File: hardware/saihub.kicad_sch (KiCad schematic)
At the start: 55 parts, among them J1 USB4105-GF-A, J2 1x12 2.54mm right-angle, Q1 AO3400A, SW1 BOOT, U1 USBLC6-2SC6, U2 SGM6232YPS8G/TR, U3 ESPC5-32E-H4, U4 TPS2553DBVR, U5 TPS2553DBVR

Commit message: feat(hardware): add header protection and refresh board deliverables
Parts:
- removed R13, R14: 10k, Saihub:R_0603_1608Metric, symbol Saihub:R
- added C21: 100n, Saihub:C_0603_1608Metric, symbol Saihub:C
- added U10: USBLC6-2SC6, Saihub:SOT-23-6, symbol Saihub:USBLC6_2SC6
- added U6, U7: TPD4E05U06DQAR, Saihub:TPD4E05U06_DQA, symbol Saihub:TPD4E05U06
- D3: value SS14 -> SS34; MPN SS14 -> SS34
- R10, R12, R9: value 100k -> 10k; MPN 100k -> 10k
- U4, U5: value TPS2553DBVR -> TPS2553DDBVR; MPN TPS2553DBVR -> TPS2553DDBVR
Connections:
- net FAULT4: now also U3.19 (GPIO15)
- net FAULT5: now also U3.5 (GPIO3)
- net GND: now also C21.2, U10.2 (GND), U6.3 (GND), U6.8 (GND), U7.3 (GND), U7.8 (GND)
- net IO0: now also U6.1 (IO1)
- net IO1: now also U6.2 (IO2)
- net IO2: now also U6.4 (IO3)
- net IO3: now also U6.5 (IO4)
- net IO4: now also U7.1 (IO1)
- net IO5: now also U7.2 (IO2)
- net IO6: now also U7.4 (IO3)
- net IO7: now also U7.5 (IO4)
- net V3_SW: now also U10.1 (IO1), U10.6 (IO1)
- net V5: now also C21.1, U10.5 (VBUS)
- net V5_SW: now also U10.3 (IO2), U10.4 (IO2)
- no-connect marks 12 -> 18
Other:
- note added: "07 HEADER ESD / SHUNT PROTECTION"
- note added: "48 x 28 mm PCB - top-side component assembly."
- note added: "FAULT4 -> input 15; FAULT5 -> input 3. Active LOW."
- note added: "Fault inputs: firmware must enable internal pullups."
- note added: "IO0-IO7: 3.3 V only; final-board ESD test required."
- note added: "Place arrays and bypass capacitors directly beside J2."
- note added: "Short, wide ground returns; qualify ESD on final PCB."
- note added: "U10: switched rails. Power current bypasses the array."
- note added: "U6/U7: four channels each; no supply or bypass needed."

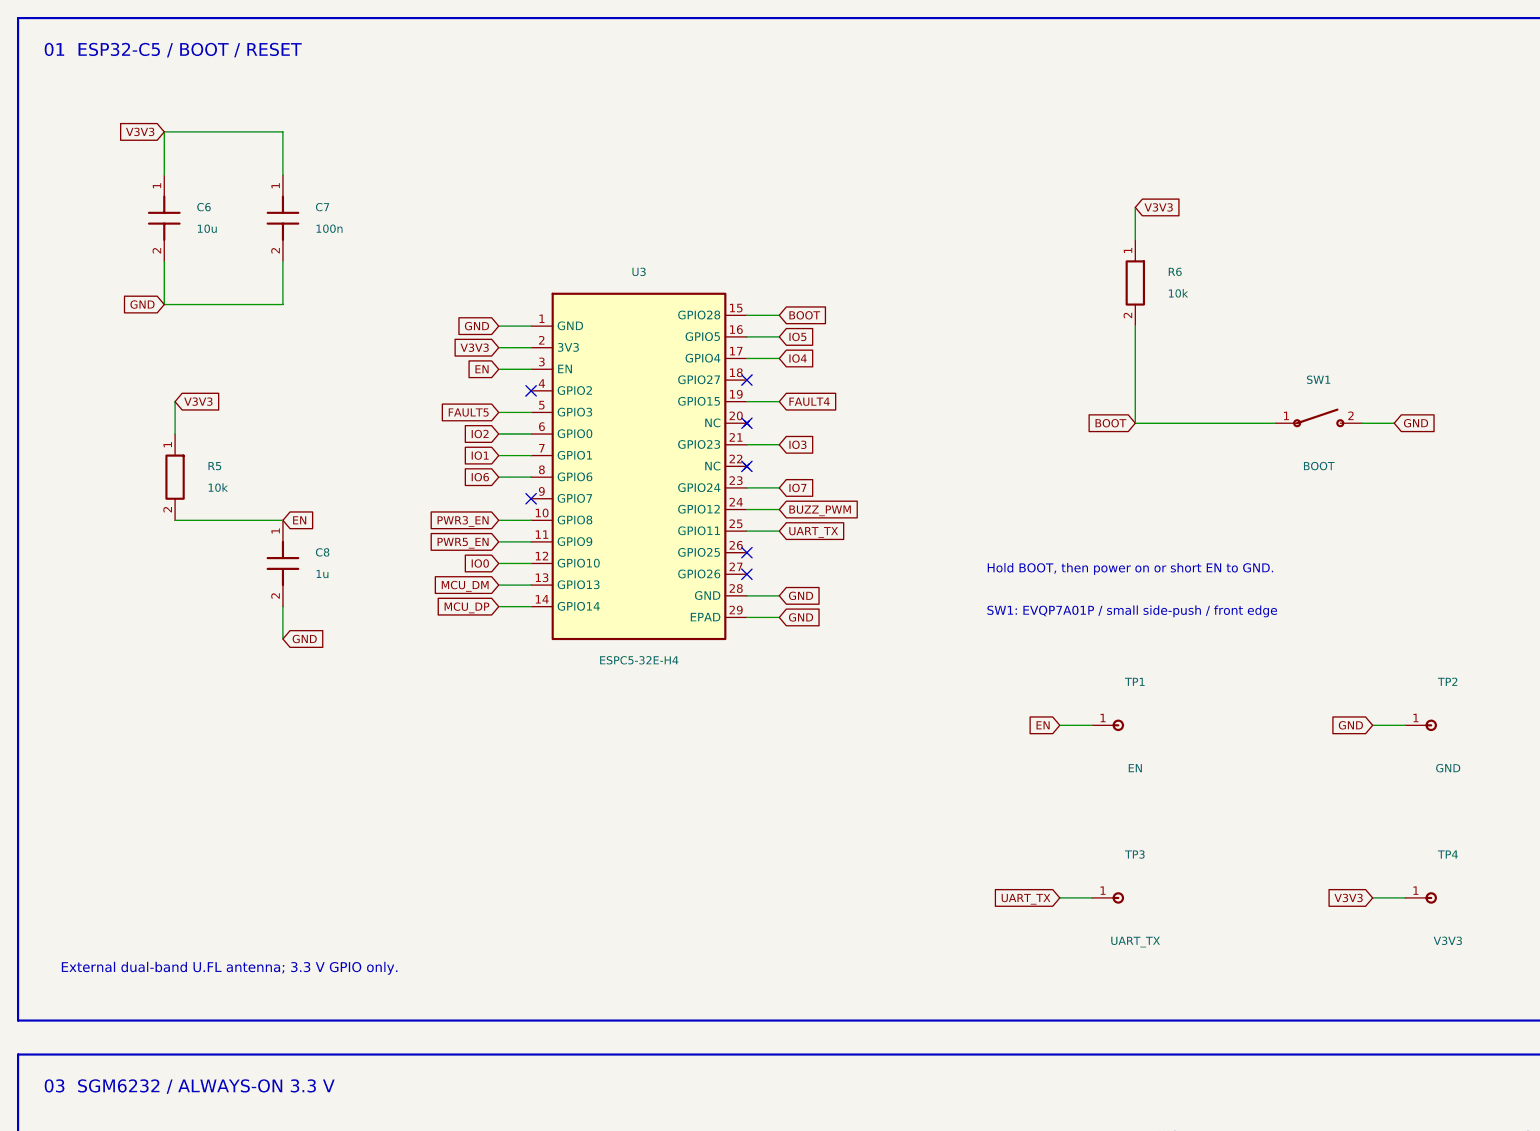
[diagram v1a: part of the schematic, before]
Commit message: Replace button and add corner antenna module without enlarging PCB
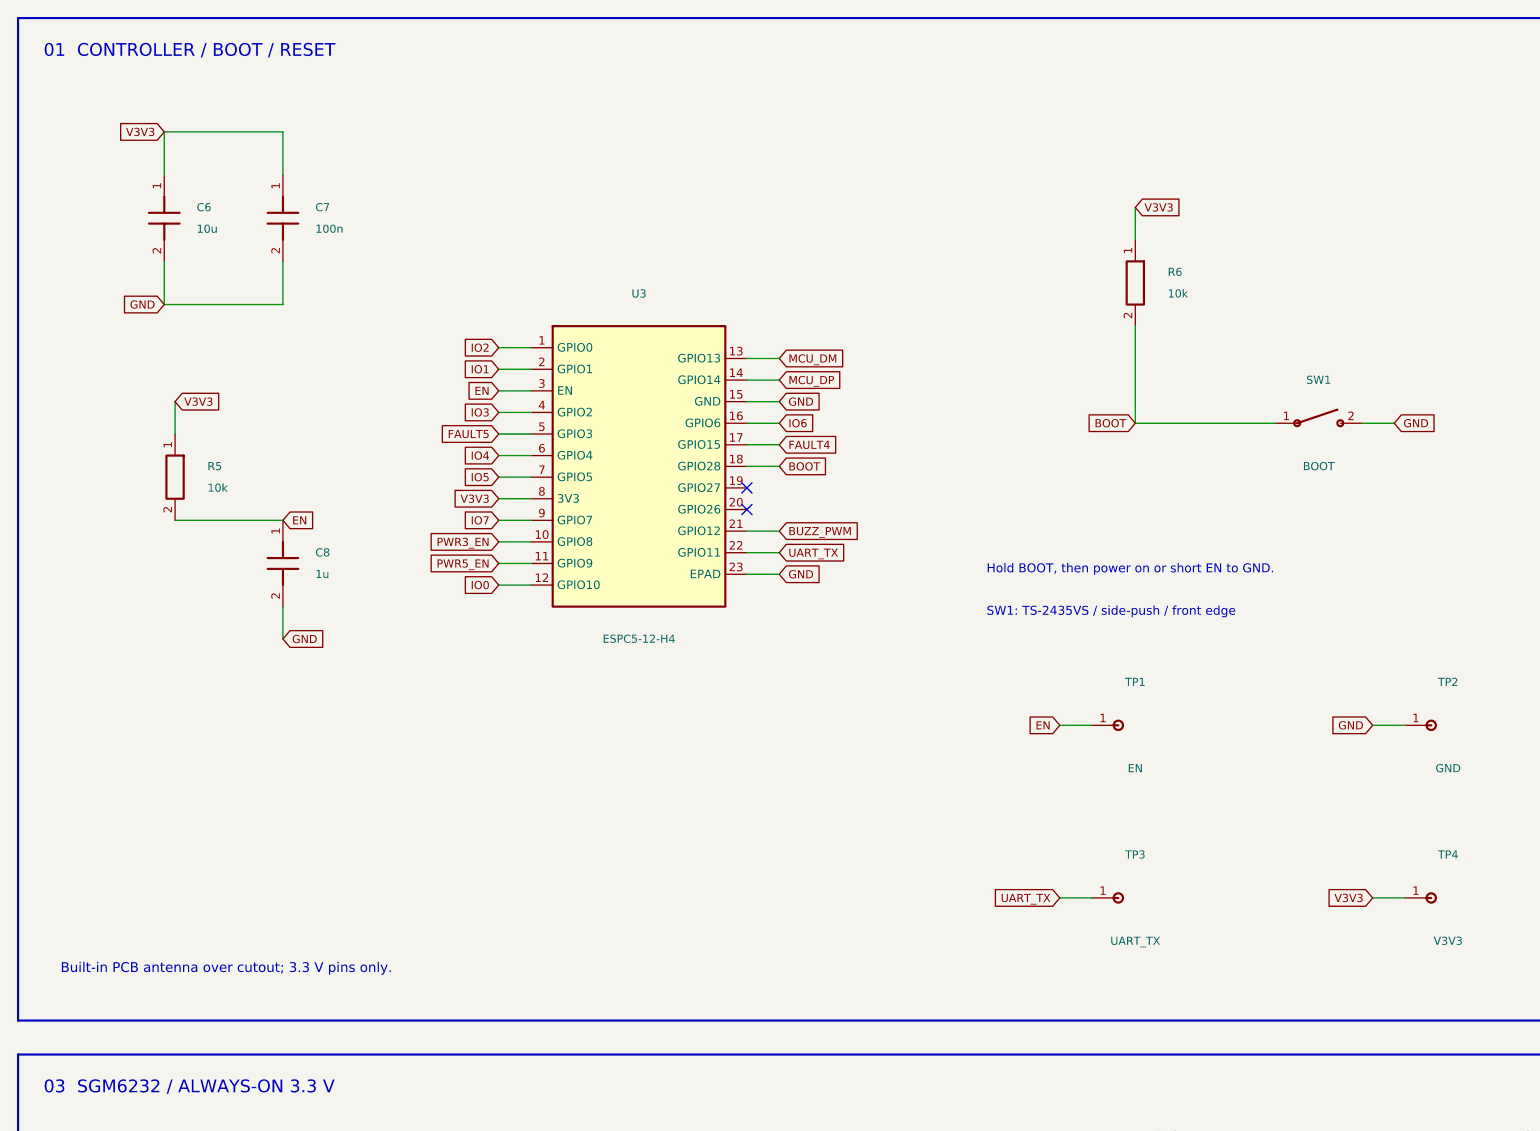
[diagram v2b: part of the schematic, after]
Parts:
- SW1: footprint Saihub:SW_SPST_EVQP7A -> Saihub:SW_SPST_TS2435VS; MPN EVQP7A01P -> TS-2435VS
- U3: value ESPC5-32E-H4 -> ESPC5-12-H4; footprint Saihub:ESPC5-32E-H4 -> Saihub:ESPC5-12-H4; symbol Saihub:ESPC5_32E_H4 -> Saihub:ESPC5_12_H4; MPN ESPC5-32E-H4 -> ESPC5-12-H4
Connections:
- net BOOT: now also U3.18 (GPIO28); no longer U3.15 (GPIO28)
- net BUZZ_PWM: now also U3.21 (GPIO12); no longer U3.24 (GPIO12)
- net FAULT4: now also U3.17 (GPIO15); no longer U3.19 (GPIO15)
- net GND: now also U3.15 (GND), U3.23 (EPAD); no longer U3.1 (GND), U3.28 (GND), U3.29 (EPAD)
- net IO1: now also U3.2 (GPIO1); no longer U3.7 (GPIO1)
- net IO2: now also U3.1 (GPIO0); no longer U3.6 (GPIO0)
- net IO3: now also U3.4 (GPIO2); no longer U3.21 (GPIO23)
- net IO4: now also U3.6 (GPIO4); no longer U3.17 (GPIO4)
- net IO5: now also U3.7 (GPIO5); no longer U3.16 (GPIO5)
- net IO6: now also U3.16 (GPIO6); no longer U3.8 (GPIO6)
- net IO7: now also U3.9 (GPIO7); no longer U3.23 (GPIO24)
- net UART_TX: now also U3.22 (GPIO11); no longer U3.25 (GPIO11)
- net V3V3: now also U3.8 (3V3); no longer U3.2 (3V3)
- no-connect marks 18 -> 13
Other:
- note added: "01 CONTROLLER / BOOT / RESET"
- note added: "Built-in PCB antenna over cutout; 3.3 V pins only."
- note added: "SW1: TS-2435VS / side-push / front edge"
- note removed: "01 ESP32-C5 / BOOT / RESET"
- note removed: "External dual-band U.FL antenna; 3.3 V GPIO only."
- note removed: "SW1: EVQP7A01P / small side-push / front edge"
- title: SAIHub-Mini - ESP32-C5 GPIO CONTROLLER -> SAIHub-Mini - IO CONTROLLER

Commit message: feat(hardware): add grouped indicators and reproducible routing
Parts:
- added D4, D5: GREEN, Saihub:LED_AA1608, symbol Saihub:LED
- added D6: RED, Saihub:LED_AA1608, symbol Saihub:LED
- added D7: BLUE, Saihub:LED_AA1608, symbol Saihub:LED
- added R19: 680, Saihub:R_0603_1608Metric, symbol Saihub:R
- added R20, R21: 1.5k, Saihub:R_0603_1608Metric, symbol Saihub:R
- added R22: 330, Saihub:R_0603_1608Metric, symbol Saihub:R
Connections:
- net GND: now also D4.1 (K), D5.1 (K), D6.1 (K), D7.1 (K)
- net V3_SW: now also R19.1
- net V5: now also R21.1
- net V5_SW: now also R20.1
- net STATUS_LED: now reaches U3.20 (GPIO26)
- net STATUS_LED: now also R22.1
- new net D4_A: D4.2 (A), R19.2
- new net D5_A: D5.2 (A), R20.2
- new net D6_A: D6.2 (A), R21.2
- new net D7_A: D7.2 (A), R22.2
- no-connect marks 13 -> 12
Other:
- note added: "08 GROUPED STATUS INDICATORS"
- note added: "48 x 28 mm PCB - LEDs top; eight resistors bottom."
- note added: "Blue: control pin 26, HIGH = on. 3V3/5V: switched rails."
- note removed: "48 x 28 mm PCB - top-side component assembly."

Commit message: fix(hardware): correct assembly footprints and package outlines
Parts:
- BZ1: value KLJ-5020 3.3V -> 5020 3V 4kHz; footprint Saihub:KLJ-5020 -> Saihub:Buzzer_5020_Supplied; MPN KLJ-5020 -> 5020 supplied specification (MPN unspecified)
- D4, D5: footprint Saihub:LED_AA1608 -> Saihub:LED_0603_1608Metric; MPN AA1608LCGSK -> KT-0603G
- D6: footprint Saihub:LED_AA1608 -> Saihub:LED_0603_1608Metric; MPN AA1608LSURSK -> KT-0603R
- D7: footprint Saihub:LED_AA1608 -> Saihub:LED_0603_1608Metric; MPN AA1608LQBS/D-295V -> KT-0603B
- R19: value 680 -> 330; MPN 680 -> 330
- R20: value 1.5k -> 1.2k; MPN 1.5k -> 1.2k
- SW1: footprint Saihub:SW_SPST_TS2435VS -> Saihub:SW_SPST_2X4_LocatingPins; MPN TS-2435VS -> 2X4
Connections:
- net D4_A: now also D4.1 (A); no longer D4.2 (A)
- net D5_A: now also D5.1 (A); no longer D5.2 (A)
- net D6_A: now also D6.1 (A); no longer D6.2 (A)
- net D7_A: now also D7.1 (A); no longer D7.2 (A)
- net GND: now also D4.2 (K), D5.2 (K), D6.2 (K), D7.2 (K); no longer D4.1 (K), D5.1 (K), D6.1 (K), D7.1 (K)
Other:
- note added: "SW1: 2X4 / locating posts / front edge"
- note removed: "SW1: TS-2435VS / side-push / front edge"

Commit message: fix(hardware): finish front-only PCB routing and review exports
Place all components and test pads on the front surface while preserving
the shell-critical connector, button, module and indicator positions.
Consolidate the four indicator resistors to 660 ohms, use the smaller
shared protection array at U10, and relocate support parts for local routing.

Complete all signal and ground connections, preserve the supply paths,
and capture replayable copper with the actual pour settings. Refresh the
schematic, interactive BOM, PCB and enclosure review documents.

Validation: zero ERC, DRC, schematic-parity and unconnected findings;
routing reconstruction passes; all six PDF pages visually reviewed.
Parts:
- removed C21: 100n, Saihub:C_0603_1608Metric, symbol Saihub:C
- R19, R22: value 330 -> 660; MPN 330 -> 660
- R20: value 1.2k -> 660; MPN 1.2k -> 660
- R21: value 1.5k -> 660; MPN 1.5k -> 660
- U10: value USBLC6-2SC6 -> TPD4E05U06DQAR; footprint Saihub:SOT-23-6 -> Saihub:TPD4E05U06_DQA; symbol Saihub:USBLC6_2SC6 -> Saihub:TPD4E05U06; MPN USBLC6-2SC6 -> TPD4E05U06DQAR
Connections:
- net GND: now also U10.3 (GND), U10.8 (GND); no longer U10.2 (GND)
- net V3_SW: no longer U10.6 (IO1)
- net V5: no longer U10.5 (VBUS)
- net V5_SW: now also U10.5 (IO4); no longer U10.3 (IO2), U10.4 (IO2)
- no-connect marks 12 -> 18
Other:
- note added: "06 HEADER / ESD / SHUNT PROTECTION"
- note added: "07 GROUPED STATUS INDICATORS"
- note added: "48 x 28 mm PCB - all components on front surface."
- note added: "Place protection arrays directly beside J2."
- note removed: "06 12-PIN MALE HEADER"
- note removed: "07 HEADER ESD / SHUNT PROTECTION"
- note removed: "08 GROUPED STATUS INDICATORS"
- note removed: "48 x 28 mm PCB - LEDs top; eight resistors bottom."
- note removed: "Place arrays and bypass capacitors directly beside J2."
- moved on the sheet: BZ1, C10, C13, C14, C15, C16, C9, D3, D4, D5, D6, D7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
